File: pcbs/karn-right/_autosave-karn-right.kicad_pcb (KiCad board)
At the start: 2 copper layers, 139.3 x 98 mm, 45 parts, among them J1 S2B-PH-K-SLFSN, SW11 SW_Push, SW12 SW_Push, SW13 SW_Push, SW14 SW_Push, SW15 SW_Push, SW21 SW_Push, SW22 SW_Push, SW23 SW_Push, SW24 SW_Push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

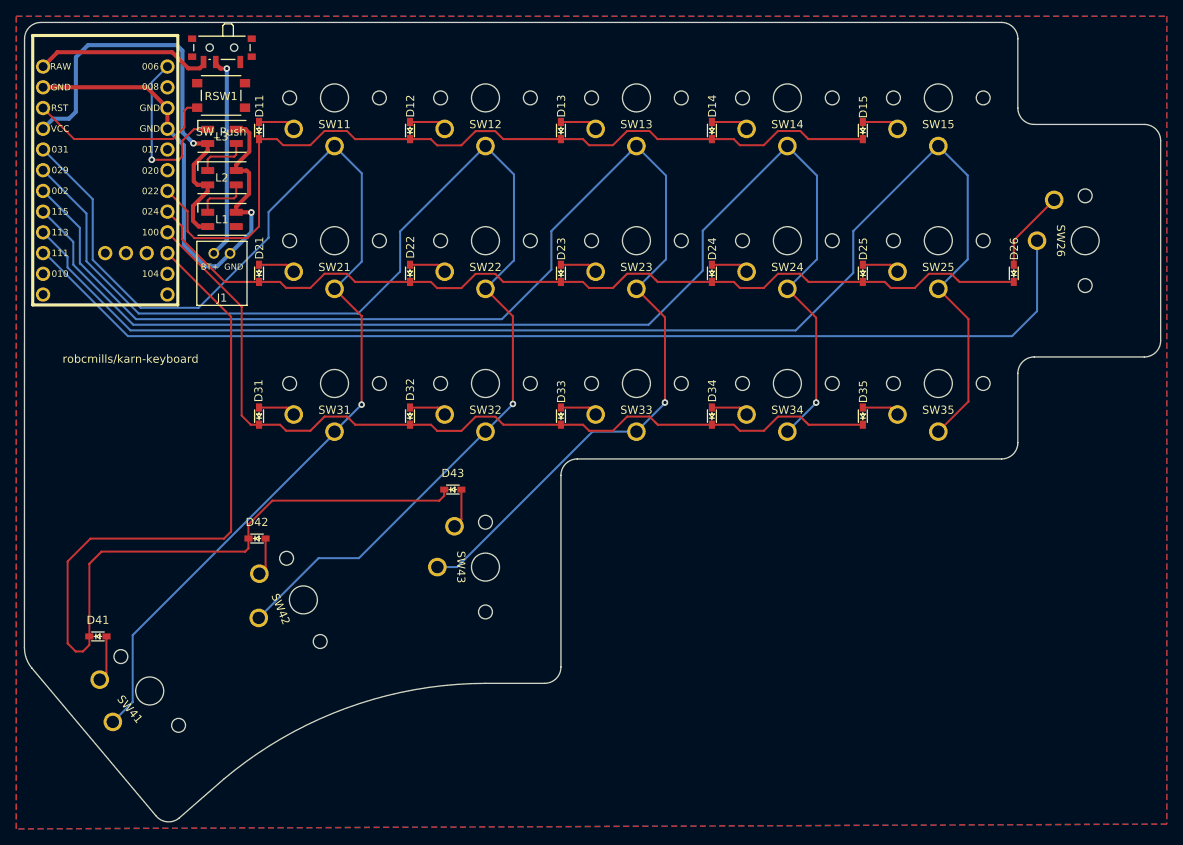
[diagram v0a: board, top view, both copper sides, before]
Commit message: Update karn-left pcb
- Apply various fixes from lessons learned on karn-right
- Fix incorrectly oriented reset switch
- Swap incorrect default polarity of JST connector footprint
- Increase size of diode pads
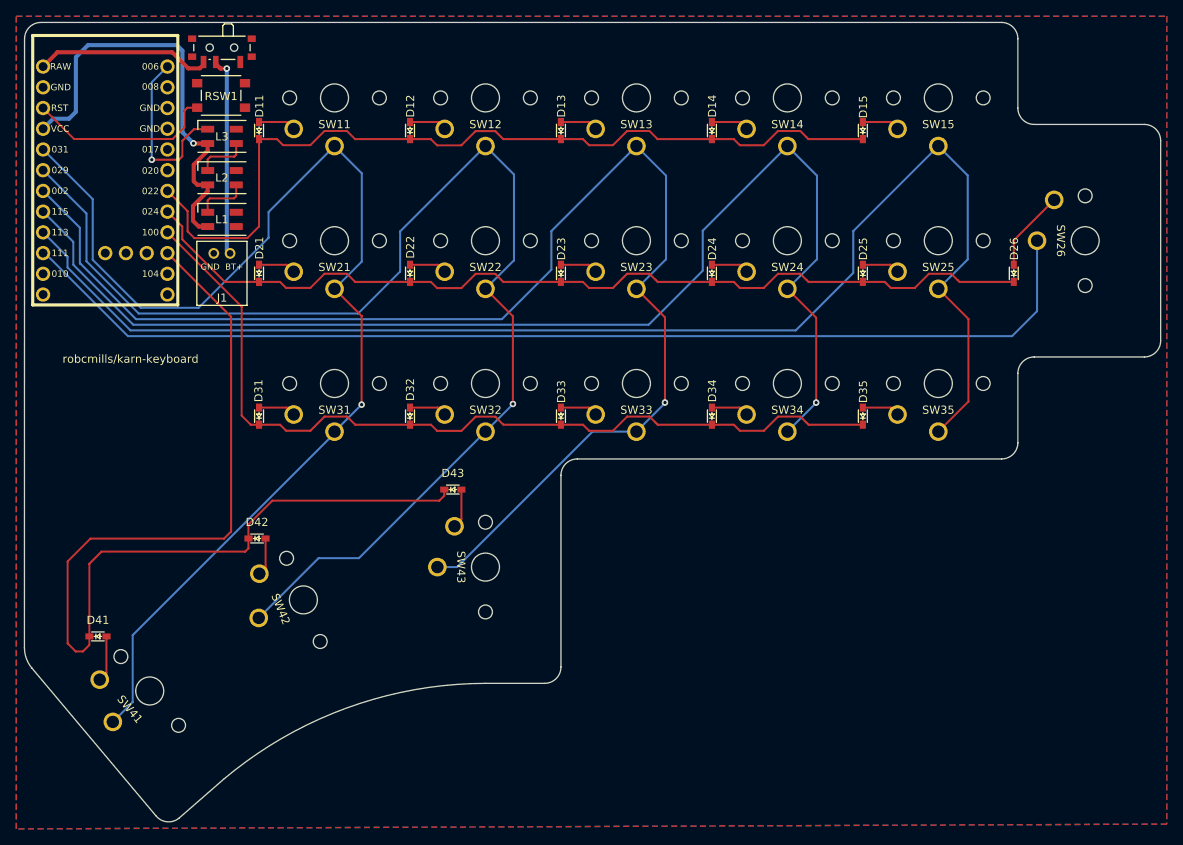
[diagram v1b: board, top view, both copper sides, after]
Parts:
- D11, D12, D13, D14, D15, D21, D22, D23, D24, D25, D26, D31, D32, D33, D34, D35, D41, D42, D43: footprint Diode_SMD:1N4148X-TP -> karn-kicad:diode-smd-1N4148X-TP
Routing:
- net GND: track 63.5 -> 0.00 mm, vias 1 -> 0
